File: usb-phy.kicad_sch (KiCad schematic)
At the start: 105 parts, among them J12 614004184726, Q17 BSS138PW, U15 TPS7B8133DRVR, U16 TPD4E05U06QDQARQ1, U17 TPD4E05U06QDQARQ1, U18 SN74HC595D, U19 MAX3421EETJ+, U20 FT4232H-56Q, U21 TPD4E05U06QDQARQ1, U22 TXU0304BQAR, U23 TXU0304BQAR, U24 TXU0304BQAR, U25 TUSB1106RSVR, Y1 ABM8G-12.000MHZ-18-D2Y-T, Y2 ABM8G-12.000MHZ-18-D2Y-T

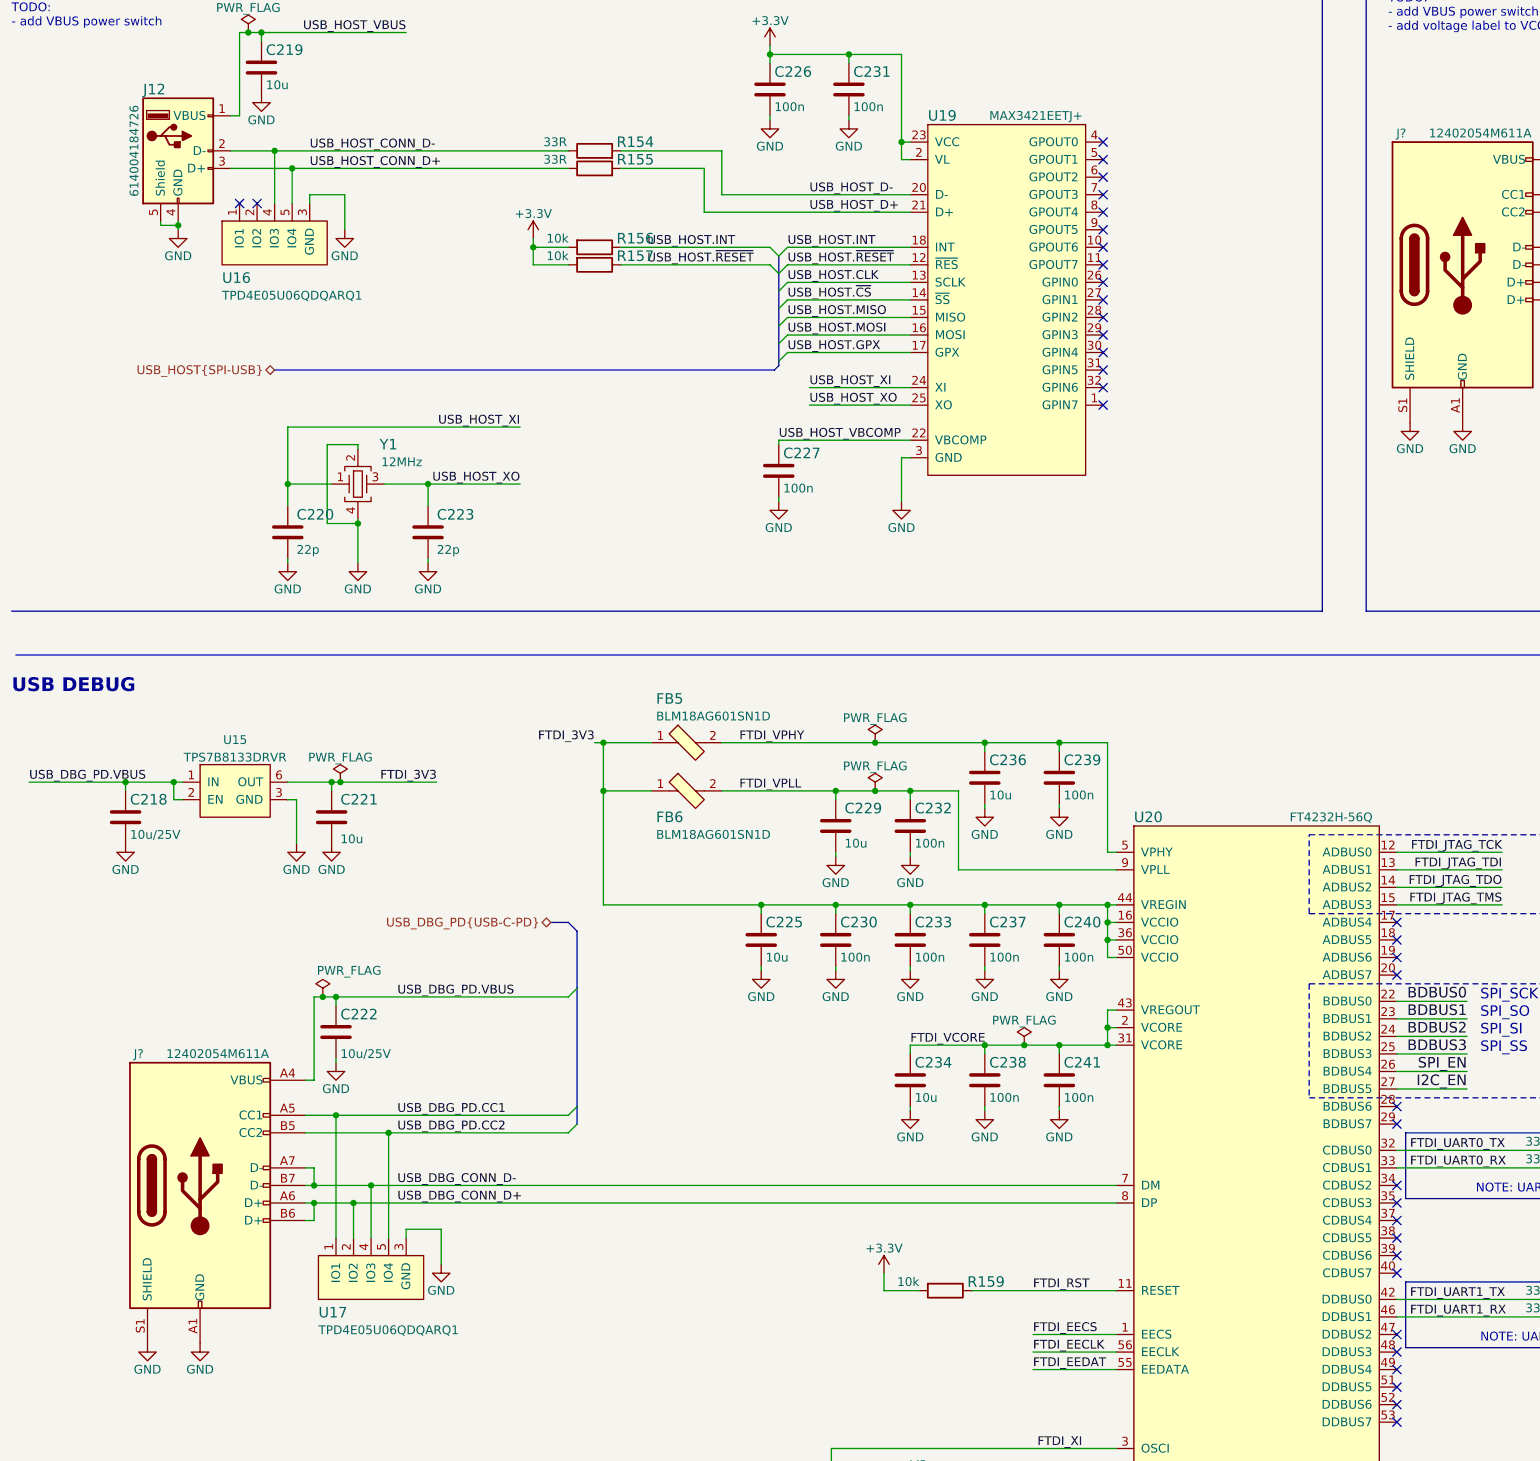
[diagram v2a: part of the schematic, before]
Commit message: Fix libs, sync schematic with PCB
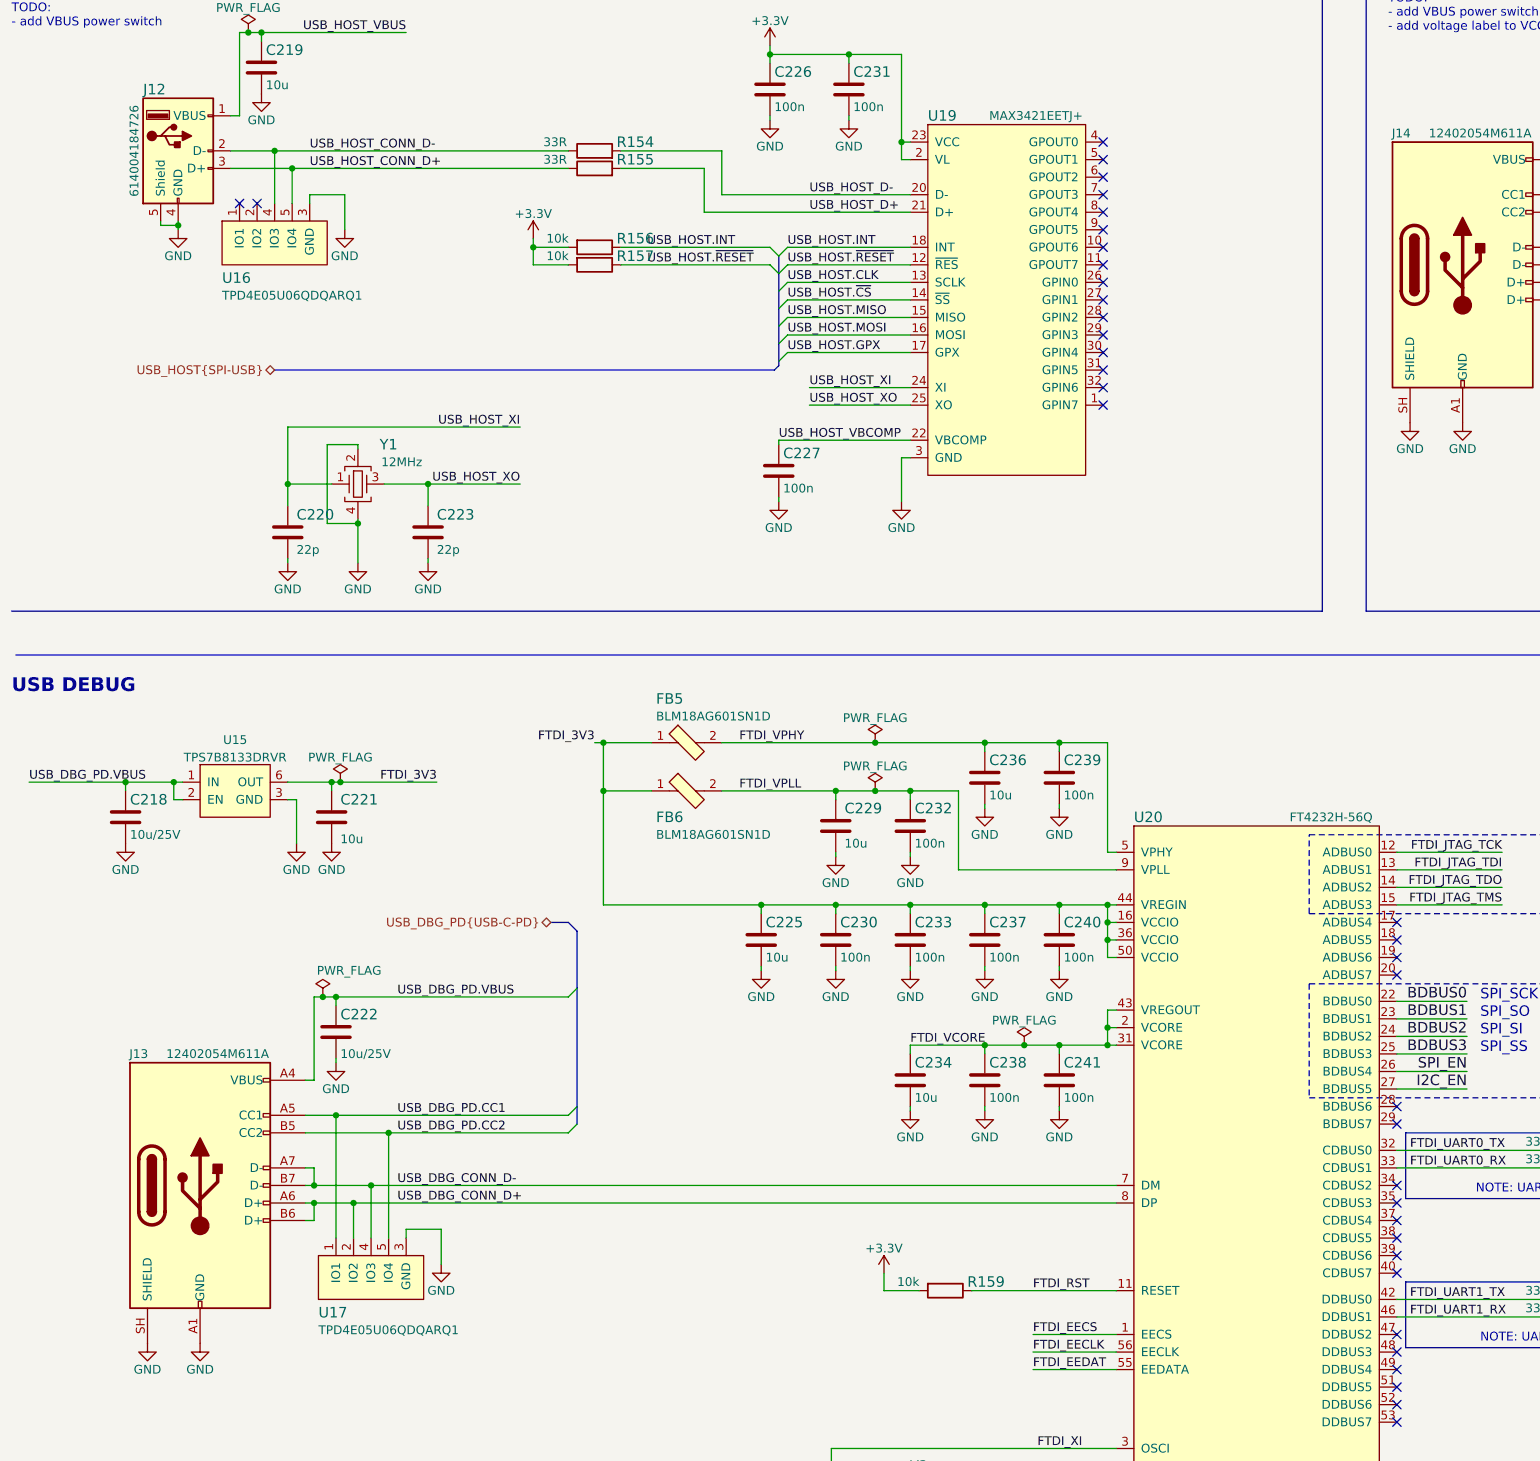
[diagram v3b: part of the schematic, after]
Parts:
- gave numbers to parts that had none: 2
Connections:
- net GND: now also J13.SH (SHIELD), J14.SH (SHIELD); no longer J13.S1 (SHIELD), J14.S1 (SHIELD)
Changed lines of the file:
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@@
     (pin "2")
   )
-  (symbol (lib_id "antmicroUSBDVIHDMIConnectors:12402054M611A") (at 40.64 191.77 0) (unit 1)
-    (in_bom yes) (on_board yes)
-    (property "Reference" "J?" (id 0) (at 31.75 172.72 0))
+  (symbol (lib_name "12402054M611A_1") (lib_id "antmicroUSBDVIHDMIConnectors:12402054M611A") (at 40.64 191.77 0) (unit 1)
+    (in_bom yes) (on_board yes)
+    (property "Reference" "J13" (id 0) (at 31.75 172.72 0))
     (property "Value" "12402054M611A" (id 1) (at 43.18 172.72 0))
     (property "Footprint" "antmicro-footprints:12402054M611A" (id 2) (at 24.13 172.72 0)
@@
     (pin "B7")
     (pin "B9")
-    (pin "S1")
+    (pin "SH")
   )
   (symbol (lib_id "power:GND") (at 165.1 137.16 0) (mirror y) (unit 1)
@@
   (symbol (lib_id "antmicroUSBDVIHDMIConnectors:12402054M611A") (at 223.52 58.42 0) (unit 1)
     (in_bom yes) (on_board yes)
-    (property "Reference" "J?" (id 0) (at 214.63 39.37 0))
+    (property "Reference" "J14" (id 0) (at 214.63 39.37 0))
     (property "Value" "12402054M611A" (id 1) (at 226.06 39.37 0))
     (property "Footprint" "antmicro-footprints:12402054M611A" (id 2) (at 207.01 39.37 0)
@@
     (pin "B7")
     (pin "B9")
-    (pin "S1")
+    (pin "SH")
   )
   (symbol (lib_id "antmicroResistors0402:R_33R_0402") (at 341.63 140.97 0) (unit 1)

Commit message: Manually import changes from pcb-wip branch
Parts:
- removed J13, J14: 12402054M611A, antmicro-footprints:12402054M611A, symbol antmicroUSBDVIHDMIConnectors:12402054M611A
- added J13, J14: USB4105-GF-A, antmicro-footprints:GCT_USB4105-GF-A, symbol antmicroUSBDVIHDMIConnectors:USB4105-GF-A
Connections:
- net GND: now also J13.A1 (GND), J13.A12 (GND), J13.B1 (GND), J13.B12 (GND), J13.S1 (SHIELD), J14.A1 (GND), J14.A12 (GND), J14.B1 (GND), J14.B12 (GND), J14.S1 (SHIELD)
- net USB_DBG_CONN_D+: now also J13.A6 (D+), J13.B6 (D+)
- net USB_DBG_CONN_D-: now also J13.A7 (D-), J13.B7 (D-)
- net USB_DBG_PD.CC1: now also J13.A5 (CC1)
- net USB_DBG_PD.CC2: now also J13.B5 (CC2)
- net USB_DBG_PD.VBUS: now also J13.A4 (VBUS), J13.A9 (VBUS), J13.B4 (VBUS), J13.B9 (VBUS)
- net USB_USR_CC1: now also J14.A5 (CC1)
- net USB_USR_CC2: now also J14.B5 (CC2)
- net USB_USR_CONN_D+: now also J14.A6 (D+), J14.B6 (D+)
- net USB_USR_CONN_D-: now also J14.A7 (D-), J14.B7 (D-)
- net USB_USR_VBUS: now also J14.A4 (VBUS), J14.A9 (VBUS), J14.B4 (VBUS), J14.B9 (VBUS)
- no-connect marks 43 -> 47
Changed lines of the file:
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@@
   (no_connect (at 213.995 236.22))
   (no_connect (at 171.45 63.5))
+  (no_connect (at 238.76 73.66))
+  (no_connect (at 55.88 207.01))
   (no_connect (at 213.995 204.47))
   (no_connect (at 171.45 71.12))
@@
   (no_connect (at 213.995 223.52))
   (no_connect (at 46.355 49.53))
+  (no_connect (at 55.88 204.47))
   (no_connect (at 79.375 262.255))
   (no_connect (at 213.995 220.98))
@@
   (no_connect (at 171.45 58.42))
   (no_connect (at 171.45 50.8))
+  (no_connect (at 238.76 71.12))
   (no_connect (at 331.47 213.36))
   (no_connect (at 171.45 43.18))
@@
     (pin "1")
   )
+  (symbol (lib_id "antmicroUSBDVIHDMIConnectors:USB4105-GF-A") (at 40.64 191.77 0) (unit 1)
+    (in_bom yes) (on_board yes)
+    (property "Reference" "J13" (id 0) (at 31.75 172.72 0))
+    (property "Value" "USB4105-GF-A" (id 1) (at 43.18 172.72 0))
+    (property "Footprint" "antmicro-footprints:GCT_USB4105-GF-A" (id 2) (at 24.13 172.72 0)
+      (effects (font (size 1.27 1.27)) (justify left bottom) hide)
+    )
+    (property "Datasheet" "https://gct.co/files/drawings/usb4105.pdf" (id 3) (at 40.64 191.77 0)
+      (effects (font (size 1.27 1.27)) (justify left bottom) hide)
+    )
+    (property "Manufacturer" "GCT" (id 4) (at 24.13 171.45 0)
+      (effects (font (size 1.27 1.27)) (justify left bottom) hide)
+    )
+    (property "MPN" "USB4105-GF-A" (id 5) (at 31.75 168.91 0)
+      (effects (font (size 1.27 1.27)) hide)
+    )
+    (pin "A1")
+    (pin "A12")
+    (pin "A4")
+    (pin "A5")
+    (pin "A6")
+    (pin "A7")
+    (pin "A8")
+    (pin "A9")
+    (pin "B1")
+    (pin "B12")
+    (pin "B4")
+    (pin "B5")
+    (pin "B6")
+    (pin "B7")
+    (pin "B8")
+    (pin "B9")
+    (pin "S1")
+  )
   (symbol (lib_id "antmicroInterfaceControllers:MAX3421EETJ+") (at 158.75 60.96 0) (unit 1)
     (in_bom yes) (on_board yes)
@@
     (pin "2")
   )
-  (symbol (lib_name "12402054M611A_1") (lib_id "antmicroUSBDVIHDMIConnectors:12402054M611A") (at 40.64 191.77 0) (unit 1)
-    (in_bom yes) (on_board yes)
-    (property "Reference" "J13" (id 0) (at 31.75 172.72 0))
-    (property "Value" "12402054M611A" (id 1) (at 43.18 172.72 0))
-    (property "Footprint" "antmicro-footprints:12402054M611A" (id 2) (at 24.13 172.72 0)
-      (effects (font (size 1.27 1.27)) (justify left bottom) hide)
-    )
-    (property "Datasheet" "https://cdn.amphenol-cs.com/media/wysiwyg/files/drawing/12402054-3.pdf" (id 3) (at 40.64 191.77 0)
-      (effects (font (size 1.27 1.27)) (justify left bottom) hide)
-    )
-    (property "Manufacturer" "Amphenol" (id 4) (at 24.13 171.45 0)
-      (effects (font (size 1.27 1.27)) (justify left bottom) hide)
-    )
-    (property "MPN" "12402054M611A" (id 5) (at 31.75 168.91 0)
-      (effects (font (size 1.27 1.27)) hide)
-    )
-    (pin "A1")
-    (pin "A12")
-    (pin "A4")
-    (pin "A5")
-    (pin "A6")
-    (pin "A7")
-    (pin "A9")
-    (pin "B1")
-    (pin "B12")
-    (pin "B4")
-    (pin "B5")
-    (pin "B6")
-    (pin "B7")
-    (pin "B9")
-    (pin "SH")
-  )
   (symbol (lib_id "power:GND") (at 165.1 137.16 0) (mirror y) (unit 1)
     (in_bom yes) (on_board yes)
@@
     (pin "2")
   )
+  (symbol (lib_id "antmicroUSBDVIHDMIConnectors:USB4105-GF-A") (at 223.52 58.42 0) (unit 1)
+    (in_bom yes) (on_board yes)
+    (property "Reference" "J14" (id 0) (at 214.63 39.37 0))
+    (property "Value" "USB4105-GF-A" (id 1) (at 226.06 39.37 0))
+    (property "Footprint" "antmicro-footprints:GCT_USB4105-GF-A" (id 2) (at 207.01 39.37 0)
+      (effects (font (size 1.27 1.27)) (justify left bottom) hide)
+    )
+    (property "Datasheet" "https://gct.co/files/drawings/usb4105.pdf" (id 3) (at 223.52 58.42 0)
+      (effects (font (size 1.27 1.27)) (justify left bottom) hide)
+    )
+    (property "Manufacturer" "GCT" (id 4) (at 207.01 38.1 0)
+      (effects (font (size 1.27 1.27)) (justify left bottom) hide)
+    )
+    (property "MPN" "USB4105-GF-A" (id 5) (at 214.63 35.56 0)
+      (effects (font (size 1.27 1.27)) hide)
+    )
+    (pin "A1")
+    (pin "A12")
+    (pin "A4")
+    (pin "A5")
+    (pin "A6")
+    (pin "A7")
+    (pin "A8")
+    (pin "A9")
+    (pin "B1")
+    (pin "B12")
+    (pin "B4")
+    (pin "B5")
+    (pin "B6")
+    (pin "B7")
+    (pin "B8")
+    (pin "B9")
+    (pin "S1")
+  )
   (symbol (lib_id "power:+3.3V") (at 323.85 201.295 0) (unit 1)
     (in_bom yes) (on_board yes)
@@
     (pin "2")
   )
-  (symbol (lib_id "antmicroUSBDVIHDMIConnectors:12402054M611A") (at 223.52 58.42 0) (unit 1)
-    (in_bom yes) (on_board yes)
-    (property "Reference" "J14" (id 0) (at 214.63 39.37 0))
-    (property "Value" "12402054M611A" (id 1) (at 226.06 39.37 0))
-    (property "Footprint" "antmicro-footprints:12402054M611A" (id 2) (at 207.01 39.37 0)
-      (effects (font (size 1.27 1.27)) (justify left bottom) hide)
-    )
-    (property "Datasheet" "https://cdn.amphenol-cs.com/media/wysiwyg/files/drawing/12402054-3.pdf" (id 3) (at 223.52 58.42 0)
-      (effects (font (size 1.27 1.27)) (justify left bottom) hide)
-    )
-    (property "Manufacturer" "Amphenol" (id 4) (at 207.01 38.1 0)
-      (effects (font (size 1.27 1.27)) (justify left bottom) hide)
-    )
-    (property "MPN" "12402054M611A" (id 5) (at 214.63 35.56 0)
-      (effects (font (size 1.27 1.27)) hide)
-    )
-    (pin "A1")
-    (pin "A12")
-    (pin "A4")
-    (pin "A5")
-    (pin "A6")
-    (pin "A7")
-    (pin "A9")
-    (pin "B1")
-    (pin "B12")
-    (pin "B4")
-    (pin "B5")
-    (pin "B6")
-    (pin "B7")
-    (pin "B9")
-    (pin "SH")
-  )
   (symbol (lib_id "antmicroResistors0402:R_33R_0402") (at 341.63 140.97 0) (unit 1)

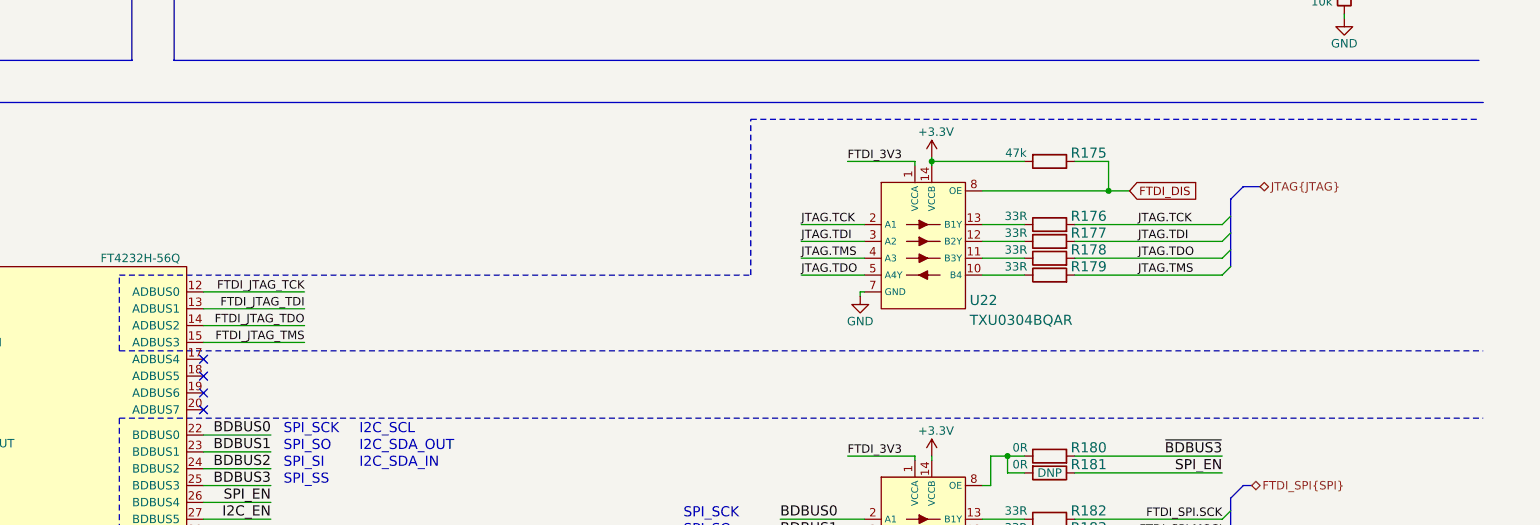
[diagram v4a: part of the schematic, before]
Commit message: Fix JTAG buffor mixed labels
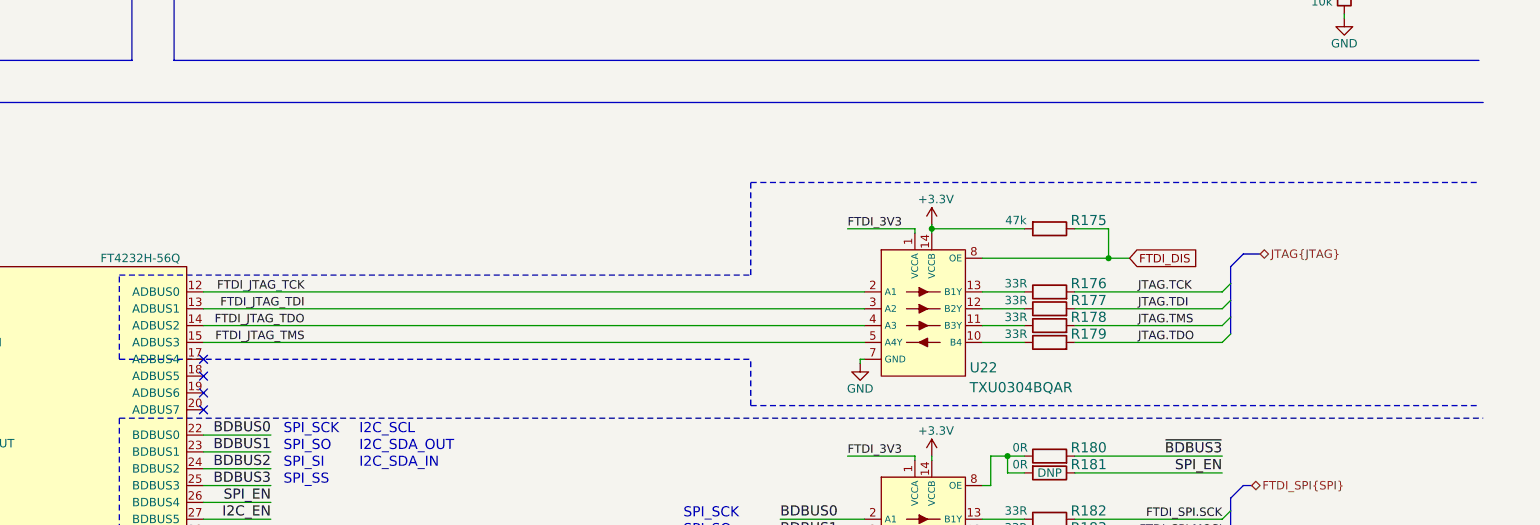
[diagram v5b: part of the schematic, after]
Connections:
- net FTDI_JTAG_TCK: now also U22.2 (A1)
- net FTDI_JTAG_TDI: now also U22.3 (A2)
- net FTDI_JTAG_TDO: now also U22.4 (A3)
- net FTDI_JTAG_TMS: now also U22.5 (A4Y)
- net JTAG.TCK: no longer U22.2 (A1)
- net JTAG.TDI: no longer U22.3 (A2)
- net JTAG.TDO: now also R179.2; no longer R178.2, U22.5 (A4Y)
- net JTAG.TMS: now also R178.2; no longer R179.2, U22.4 (A3)
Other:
- moved on the sheet: R175, R176, R177, R178, R179, U22
